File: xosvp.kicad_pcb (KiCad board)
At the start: 2 copper layers, 49.5 x 50 mm, 14 parts

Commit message: Initial Commit. Major redesign, yet to be finished.
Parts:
- removed RCA1: PJRAN3XIU03X, xosvp:PJRAN3X1U
- removed REF**: OSHW-Logo2_9.8x8mm_SilkScreen, Symbol:OSHW-Logo2_9.8x8mm_SilkScreen
- added C4: 10uF, Capacitor_SMD:CP_Elec_4x5.8, F.Cu at (26.2, 52.8)
- added C5: 0.1uF, Capacitor_SMD:C_0805_2012Metric, F.Cu at (29.7, 52.3)
- added C6: 0.1uF, Capacitor_SMD:C_0805_2012Metric, F.Cu at (34.3, 52.8)
- added R7: R75, Resistor_SMD:R_0805_2012Metric, F.Cu at (34.3, 55.4)
- added R8: 10K, Resistor_SMD:R_0805_2012Metric, F.Cu at (29.2, 49.3)
- added SYNC1: LMH1980, xosvp:LMH1980, F.Cu at (34.7, 47.6)
- added VGA2: DB15_Female_HighDensity_MountingHoles, xosvp:AHDF15A, F.Cu at (39.4, 34.0)
- moved R4 6.76 mm to (38.4, 42.7)
- moved R6 5.30 mm to (43.4, 42.7)
- moved R1 2.00 mm to (47.5, 55.4)
- moved R2 2.00 mm to (43.8, 55.4)
- moved R3 2.00 mm to (40.1, 55.4)
- moved C2 1.54 mm to (64.0, 57.9)
- moved TOSLINK1 1.54 mm to (63.0, 65.8)
- moved VGA1 1.54 mm to (39.3, 61.1)
- moved R5 1.39 mm to (40.9, 42.7)
- moved C3 1.25 mm to (46.4, 50.9)
- moved FILTER1 1.15 mm to (42.3, 49.0)
- moved C1 0.51 mm to (49.9, 50.0)
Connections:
- net PB_BLUE renamed BLUE
- net PR_RED renamed RED
- net Y_GREEN renamed GREEN
- C1 pad 2: Earth -> GND
- C2 pad 2: Earth -> GND
- C3 pad 2: Earth -> GND
- FILTER1 pad 5: Earth -> GND
- R1 pad 2: Earth -> GND
- R2 pad 2: Earth -> GND
- R3 pad 2: Earth -> GND
- TOSLINK1 pad 1: Earth -> GND
- TOSLINK1 pad 4: Earth -> unconnected-(TOSLINK1-Mount-Pad4)
- TOSLINK1 pad 5: Earth -> unconnected-(TOSLINK1-Mount-Pad5)
- VGA1 pad 0: Earth -> GND
- VGA1 pad 10: Earth -> GND
- VGA1 pad 11: Earth -> GND
- VGA1 pad 12: Earth -> GND
- VGA1 pad 14: Earth -> SW1
- VGA1 pad 15: Earth -> SW1
- VGA1 pad 4: Earth -> SYNC
- VGA1 pad 5: Earth -> GND
- VGA1 pad 6: Earth -> GND
- VGA1 pad 7: Earth -> GND
- VGA1 pad 8: Earth -> GND
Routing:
- net SPDIF: track 29.3 -> 0.00 mm
- net Net-(R5-Pad2): track 31.1 -> 6.52 mm
- net H_SYNC: track 0.00 -> 22.7 mm
- net V_SYNC: track 0.00 -> 22.1 mm
- net Net-(R4-Pad2): track 27.5 -> 6.41 mm
- net Net-(R6-Pad2): track 27.6 -> 6.63 mm
- net +5V: track 57.2 -> 67.4 mm
- net SYNC: track 0.00 -> 6.27 mm
- net Net-(FILTER1-OUT1): track 4.14 -> 9.27 mm
- net Net-(SYNC1-REXT): track 0.00 -> 3.76 mm
- net Net-(SYNC1-VIN): track 0.00 -> 3.75 mm
- net Net-(FILTER1-OUT3): track 3.95 -> 7.41 mm
- net SW1: track 0.00 -> 2.30 mm
- net BLUE: track 9.04 -> 7.11 mm
- net RED: track 9.14 -> 10.4 mm
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- added copper zone on B.Cu, net GND
- removed copper zone on B.Cu, net Earth
- removed copper zone on F.Cu, net Earth
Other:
- net class 75ohm removed
- net class Default removed
- net class med removed
- board text added: "Initial Design by Darren Thompson VGA Design by H Warfield"
- board text added: "XOSVGA"
- board text added: "{ "ViaStitching": "0.2", "stitch_zone_0": { "HSpacing": "1", "VSpacing": "1", "Clearance": "0", "Randomize": false } }"
- board text added: "{ "ViaStitching": "0.2", "stitch_zone_0": { "HSpacing": "1", "VSpacing": "1", "Clearance": "0", "Randomize": true } }"
- board text added: "{ "ViaStitching": "0.2", "stitch_zone_0": { "HSpacing": "1", "VSpacing": "1", "Clearance": "0.2", "Randomize": false } }"
- board text added: "{ "ViaStitching": "0.2", "stitch_zone_0": { "HSpacing": "1", "VSpacing": "1", "Clearance": "1", "Randomize": true } }"
- board text removed: "Designed by Darren Thompson"
- board text removed: "XOSVP HD BREAKOUT"

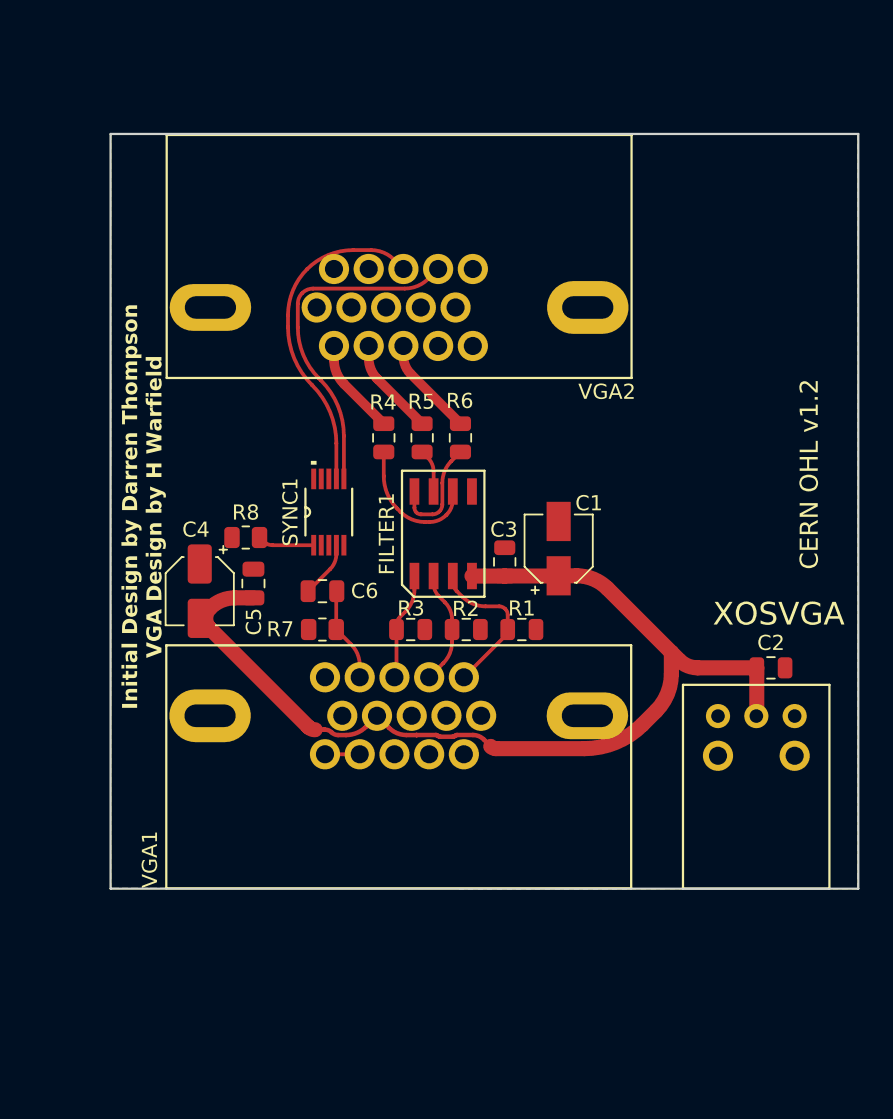
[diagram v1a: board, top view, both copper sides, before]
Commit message: Have redesigned the pcb again, realizing that the VGA connector must be flipped to prevent crossing the color signals. Have also extended the board to facilitate proper impedance matching, which was obstructed by the larger connector. Also added the 100 ohms resistors to the sync outputs as suggested by the datasheet.
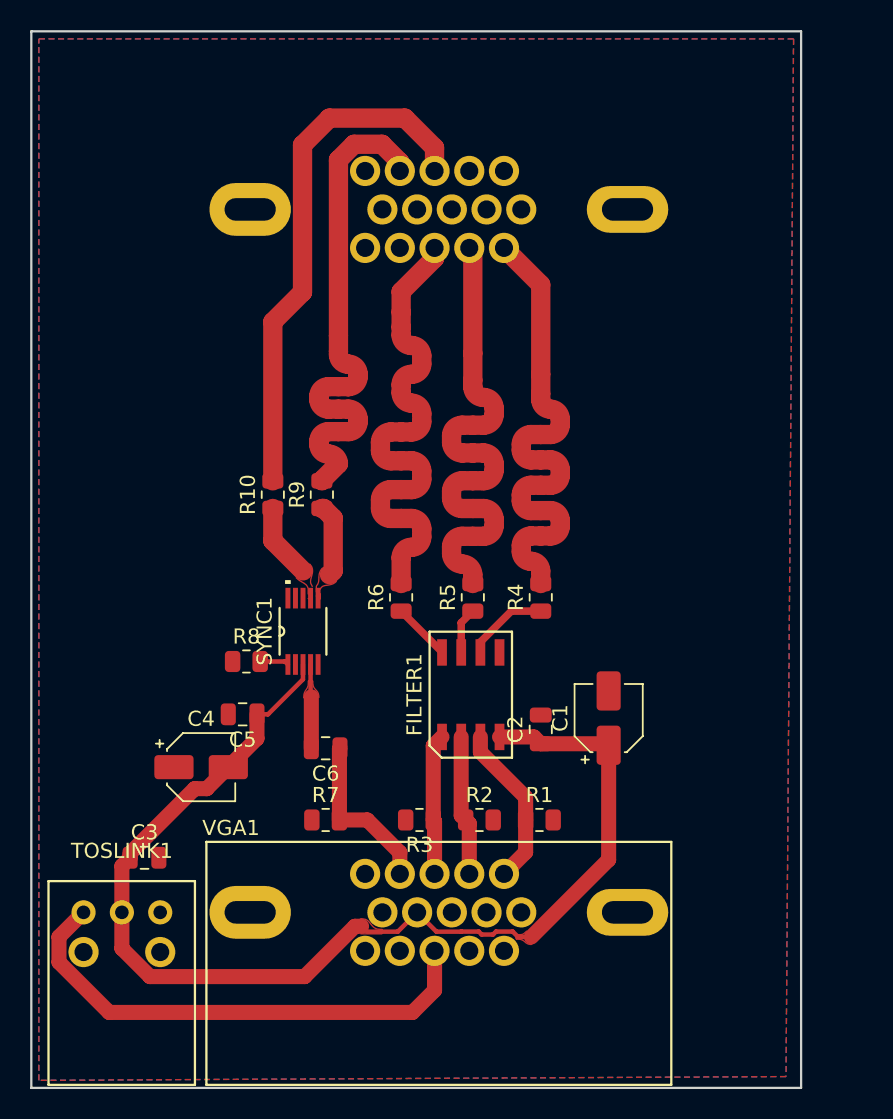
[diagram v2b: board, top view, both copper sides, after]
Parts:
- added R10: 100, Resistor_SMD:R_0805_2012Metric, F.Cu at (31.0, 46.4)
- added R9: 100, Resistor_SMD:R_0805_2012Metric, F.Cu at (34.3, 46.4)
- VGA2: moved to B.Cu
- moved TOSLINK1 44.0 mm to (21.0, 78.8)
- moved C3 30.9 mm to (22.5, 70.5), turned to 0 degrees
- moved C2 15.8 mm to (48.8, 62.0), turned to 90 degrees
- moved R4 14.8 mm to (48.8, 53.2)
- moved VGA1 13.3 mm to (42.0, 74.1)
- moved R1 12.7 mm to (48.7, 68.0)
- moved R2 12.6 mm to (44.7, 68.0)
- moved R3 12.6 mm to (40.7, 68.0), turned to 180 degrees
- moved R7 12.6 mm to (34.5, 68.0)
- moved C1 11.7 mm to (53.2, 61.2)
- moved C4 11.7 mm to (26.2, 64.5), turned to 0 degrees
- moved R6 11.3 mm to (39.5, 53.2)
- moved R5 11.1 mm to (44.2, 53.2)
- moved FILTER1 10.8 mm to (44.1, 59.7)
- moved C6 10.4 mm to (34.5, 63.2)
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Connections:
- SYNC1 pad 6: H_SYNC -> Net-(SYNC1-HS_OUT)
- SYNC1 pad 7: V_SYNC -> Net-(SYNC1-VS_OUT)
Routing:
- net SPDIF: track 0.00 -> 33.5 mm
- net Net-(R5-Pad2): track 6.52 -> 34.6 mm
- net Net-(R4-Pad2): track 6.41 -> 34.5 mm
- net Net-(R6-Pad2): track 6.63 -> 34.5 mm
- net V_SYNC: track 22.1 -> 34.9 mm
- net H_SYNC: track 22.7 -> 34.7 mm
- net +5V: track 67.4 -> 77.3 mm
- net SYNC: track 6.27 -> 11.5 mm
- net Net-(SYNC1-VS_OUT): track 0.00 -> 4.97 mm
- net Net-(SYNC1-HS_OUT): track 0.00 -> 4.87 mm
- net Net-(FILTER1-OUT1): track 9.27 -> 5.53 mm
- net Net-(FILTER1-OUT3): track 7.41 -> 3.86 mm
- net SW1: track 2.30 -> 0.00 mm
- net BLUE: track 7.11 -> 9.35 mm
- net GREEN: track 7.62 -> 9.63 mm
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- added copper zone on F.Cu, net +5V
- added copper zone on F.Cu, net GND
- added copper zone on F.Cu, net Net-(SYNC1-HS_OUT)
- added copper zone on F.Cu, net Net-(SYNC1-VIN)
- added copper zone on F.Cu, net Net-(SYNC1-VS_OUT)
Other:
- board size 49.5 x 50 mm -> 51 x 70 mm
- board text removed: "CERN OHL v1.2"
- board text removed: "Initial Design by Darren Thompson VGA Design by H Warfield"
- board text removed: "XOSVGA"
